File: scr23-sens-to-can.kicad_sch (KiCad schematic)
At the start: 55 parts, among them IC1 ADS1256IDBRG4, J1 ATM13-12PA-BM01, J2 6473711-1, SW1 SW_SPDT, U1 SRV05-4, U10 AP63205WU, U4 TJA1042T-3, U5 AP7370-33Y-13, U8 STM32G431CBT6, U9 SRV05-4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

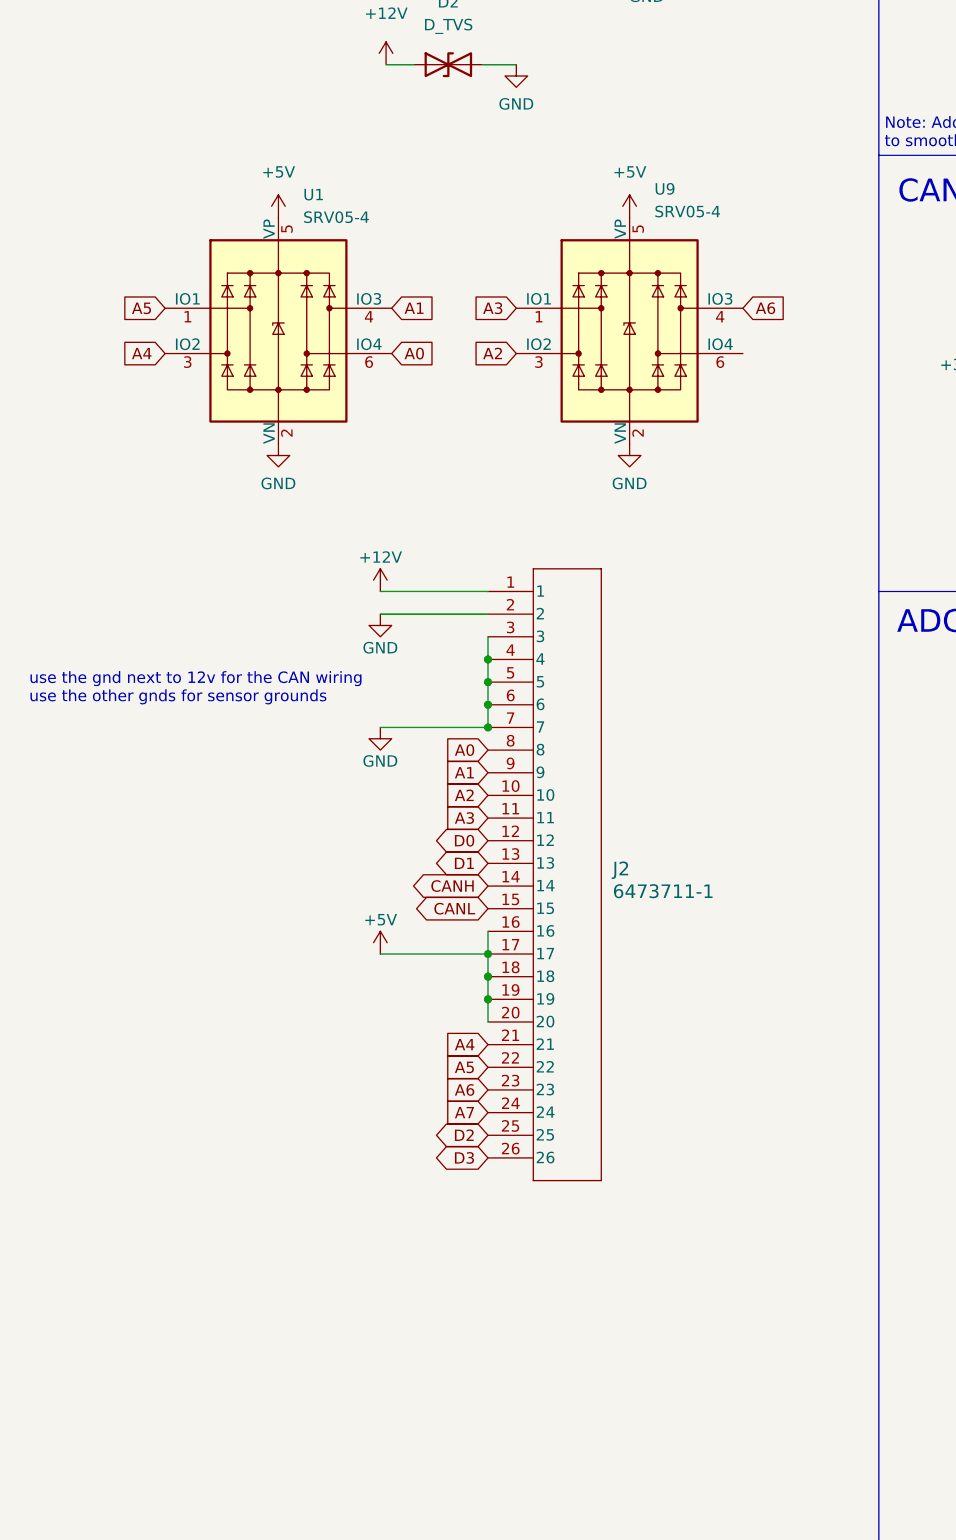
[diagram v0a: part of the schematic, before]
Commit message: add another TVS array for digital input/outputs
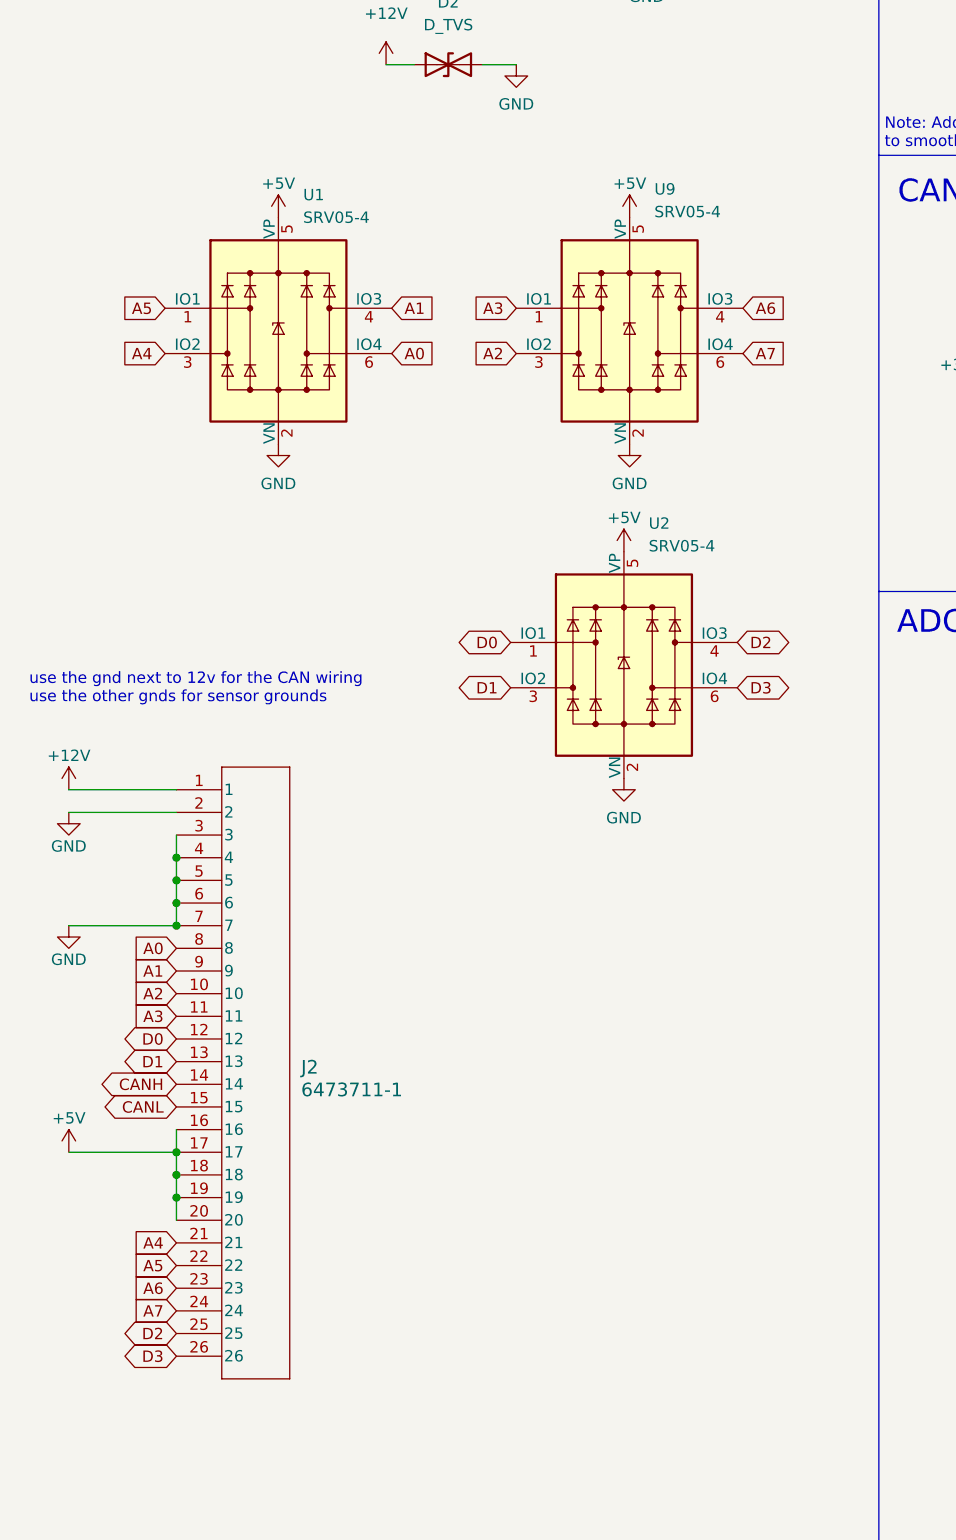
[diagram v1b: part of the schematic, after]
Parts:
- added U2: SRV05-4, Package_TO_SOT_SMD:SOT-23-6, symbol Power_Protection:SRV05-4
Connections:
- net +5V: now also U2.5 (VP)
- net A7: now also U9.6 (IO4)
- net D0: now also U2.1 (IO1)
- net D1: now also U2.3 (IO2)
- net D2: now also U2.4 (IO3)
- net D3: now also U2.6 (IO4)
- net GND: now also U2.2 (VN)
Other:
- moved on the sheet: J2

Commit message: really close to being done with schematic, need to verify stuff for ADC with page 28 of ADC datasheet
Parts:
- added C30, C31: 27pF, Capacitor_SMD:C_0603_1608Metric_Pad1.08x0.95mm_HandSolder, symbol Device:C_Small
- added J3: Conn_ST_STDC14, Connector_PinHeader_1.27mm:PinHeader_2x07_P1.27mm_Vertical_SMD, symbol Connector:Conn_ST_STDC14
- added R1: 100, Resistor_SMD:R_0603_1608Metric, symbol Device:R_Small
- added Y3: ECS-76.8-18-5PXEN-TR, ECS_76_8_18_5PXEN_TR:XTAL_ECS-76.8-18-5PXEN-TR, symbol ECS-76.8-18-5PXEN-TR:ECS-76.8-18-5PXEN-TR
- C12, C13, C14, C15, J1, Y1, Y2: now not fitted; now left out of the parts list
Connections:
- net +3.3V: now also IC1.14 (~{SYNC_}PDWN), IC1.16 (DVDD), J3.3 (VCC)
- net +3.3VA: no longer IC1.16 (DVDD)
- net D0: no longer U8.9 (PA1)
- net D1: no longer U8.10 (PA2)
- net GND: now also IC1.15 (~{RESET}), C30.2, C31.2, J3.5 (GND), J3.7 (GND), R1.1; no longer IC1.20 (~{CS})
- net SWCLK: now also J3.6 (JCLK/SWCLK)
- net SWDIO: now also J3.4 (JTMS/SWDIO)
- net SWO: now also J3.8 (JTDO/SWO)
- net XTAL2: now reaches IC1.18 (XTAL2)
- net XTAL2: now also C31.1, Y3.2
- net XTAL1: now reaches IC1.19 (XTAL1/CLKIN)
- net XTAL1: now also C30.1, Y3.1
- net ADC_CS: now reaches U8.12 (PA4)
- net ADC_CS: now also IC1.20 (~{CS})
- net NRST: now reaches U8.7 (PG10-NRST)
- net NRST: now also J3.12 (~{RST})
- new net: J3.11 (GNDDetect), R1.2
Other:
- note removed: "FDCAN pins might need to be on PB9 TX PB8 RX, dunno how that interacts with BOOT0 or how to deal with the datasheet having CANFD_RX/TX on both sets of pins??"
- moved on the sheet: C28, FB1, U8B

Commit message: one missed save, also definitely need to change vref+
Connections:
- net +3.3V: now also IC1.15 (~{RESET})
- net GND: no longer IC1.15 (~{RESET})
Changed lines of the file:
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@@
   (junction (at 165.1 198.12) (diameter 0) (color 0 0 0 0)
   )
+  (junction (at 213.36 226.06) (diameter 0) (color 0 0 0 0)
+  )
   (junction (at 309.88 203.835) (diameter 0) (color 0 0 0 0)
   )
@@
   (junction (at 409.575 126.365) (diameter 0) (color 0 0 0 0)
   )
-  (junction (at 219.075 223.52) (diameter 0) (color 0 0 0 0)
-  )
   (junction (at 132.715 72.39) (diameter 0) (color 0 0 0 0)
   )
@@
     (stroke (width 0) (type default))
   )
-  (wire (pts (xy 213.36 223.52) (xy 219.075 223.52))
+  (wire (pts (xy 213.36 223.52) (xy 224.79 223.52))
     (stroke (width 0) (type default))
   )
@@
     (stroke (width 0) (type default))
   )
-  (wire (pts (xy 213.36 228.6) (xy 219.075 228.6))
-    (stroke (width 0) (type default))
-  )
   (wire (pts (xy 347.345 46.99) (xy 333.375 46.99))
     (stroke (width 0) (type default))
@@
     (stroke (width 0) (type default))
   )
+  (wire (pts (xy 213.36 226.06) (xy 213.36 228.6))
+    (stroke (width 0) (type default))
+  )
   (wire (pts (xy 153.035 74.93) (xy 165.735 74.93))
     (stroke (width 0) (type default))
   )
-  (wire (pts (xy 219.075 223.52) (xy 224.79 223.52))
-    (stroke (width 0) (type default))
-  )
   (wire (pts (xy 330.2 175.26) (xy 340.995 175.26))
     (stroke (width 0) (type default))
   )
-  (wire (pts (xy 219.075 228.6) (xy 219.075 223.52))
-    (stroke (width 0) (type default))
-  )
